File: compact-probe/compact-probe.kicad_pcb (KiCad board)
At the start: 4 copper layers, 47.5 x 47.5 mm, 30 parts, among them J1 Conn_02x05_Counter_Clockwise, J2 SM04B-SRSS-TB(LF)(SN), J3 SM04B-SRSS-TB(LF)(SN), U1 TruStability_SPI, U2 TruStability_SPI, U3 TruStability_SPI, U4 ESP32-C3-WROOM-02-H4, U5 BMP388, U6 LT1963AxST-3.3, X1 baro_cap

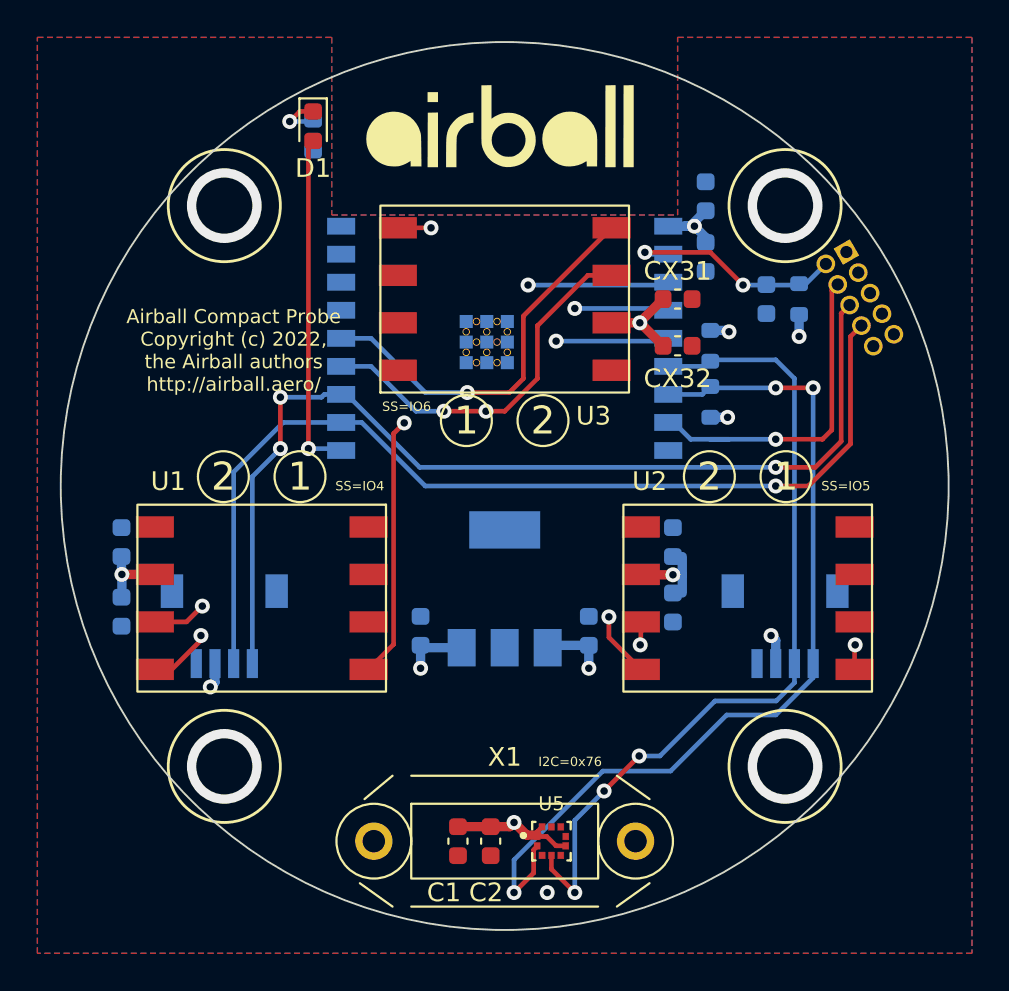
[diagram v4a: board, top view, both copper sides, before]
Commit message: Finished first cut of routing.
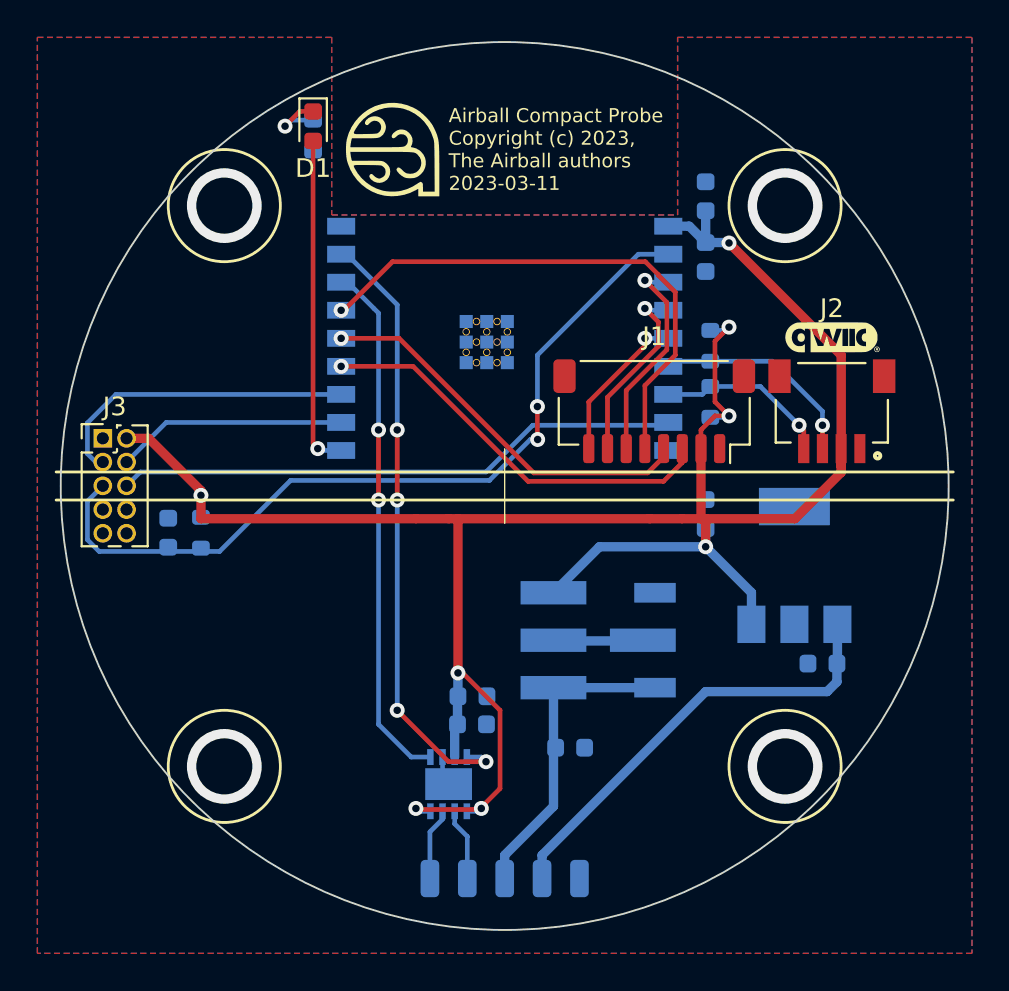
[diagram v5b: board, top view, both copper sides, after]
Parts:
- removed C2, CX12, CX22: 0.1uF, Capacitor_SMD:C_0603_1608Metric
- removed CX11, CX21, CX31, CX32: 4.7uF, Capacitor_SMD:C_0603_1608Metric
- removed the G*** at (-0.15, -18.5)
- removed U1, U2, U3: TruStability_SPI, compact-probe:TruStability SMT
- removed U5: BMP388, compact-probe:BMP388
- removed X1: baro_cap, compact-probe:baro_cap
- added C10: 22uF, Capacitor_SMD:C_0603_1608Metric, B.Cu at (-1.73, 11.2)
- added C9: 100nF, Capacitor_SMD:C_0603_1608Metric, B.Cu at (-1.75, 12.8)
- added G***: LOGO, airball-hardware:airball-logo-5mm, F.Cu at (-6.00, -18.0)
- added IC1: ATA6561-GBQW-N, airball-hardware:SON65P300X300X90-9N-D, B.Cu at (-3.00, 15.9)
- added J4: Conn_01x01_Female, Connector_Wire:SolderWirePad_1x01_SMD_1x2mm, B.Cu at (4.00, 21.0)
- added J5: Conn_01x01_Female, Connector_Wire:SolderWirePad_1x01_SMD_1x2mm, B.Cu at (2.00, 21.0)
- added J6: Conn_01x01_Female, Connector_Wire:SolderWirePad_1x01_SMD_1x2mm, B.Cu at (0.00, 21.0)
- added J7: Conn_01x01_Female, Connector_Wire:SolderWirePad_1x01_SMD_1x2mm, B.Cu at (-2.00, 21.0)
- added J8: Conn_01x01_Female, Connector_Wire:SolderWirePad_1x01_SMD_1x2mm, B.Cu at (-4.00, 21.0)
- added PS1: K7803MT-500R4, airball-hardware:CONV_K7803MT-500R4, B.Cu at (5.00, 8.25)
- C1: value 4.7uF -> 10uF; moved to B.Cu
- G***: moved to F.Cu
- J1: value Conn_02x05_Counter_Clockwise -> Conn_01x08_Male; footprint compact-probe:1.27mm_02x05_header -> airball-hardware:JST_SH_SM08B-SRSS-TB_1x08-1MP_P1.00mm_Horizontal; moved to F.Cu
- J2: value SM04B-SRSS-TB(LF)(SN) -> Conn_01x04_Male; footprint compact-probe:JST_SM04B-SRSS-TB(LF)(SN) -> airball-hardware:JST_SM04B-SRSS-TB(LF)(SN); moved to F.Cu
- J3: value SM04B-SRSS-TB(LF)(SN) -> Conn_02x05_Odd_Even; footprint compact-probe:JST_SM04B-SRSS-TB(LF)(SN) -> Connector_PinHeader_1.27mm:PinHeader_2x05_P1.27mm_Vertical; moved to F.Cu
- moved J3 38.4 mm to (-21.5, -2.55)
- moved J2 34.5 mm to (17.5, -2.00), turned to 180 degrees
- moved C4 34.4 mm to (-18.0, 2.50), turned to 90 degrees
- moved R1 34.4 mm to (-16.2, 2.50), turned to -90 degrees
- moved C5 16.5 mm to (10.8, 1.50)
- moved U6 15.6 mm to (15.5, 4.25)
- moved C3 12.6 mm to (17.0, 9.50), turned to 180 degrees
- moved J1 12.5 mm to (8.00, -4.00), turned to 180 degrees
- moved G*** 11.5 mm to (17.5, -8.00), turned to 0 degrees
- moved C1 7.81 mm to (3.50, 14.0), turned to 0 degrees
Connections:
- C1 pad 1: +3V3 -> 12V28
- C3 pad 1: +5V -> VBAT
- J1 pad 2: unconnected-(J1-Pad2) -> +3V3
- J1 pad 3: unconnected-(J1-Pad3) -> MISO
- J1 pad 4: unconnected-(J1-Pad4) -> SCLK
- J1 pad 5: +5V -> SS1
- J1 pad 6: unconnected-(J1-Pad6) -> SS2
- J1 pad 7: RXD -> SS3
- J1 pad 8: TXD -> SS4
- J2 pad 2: +5V -> +3V3
- J2 pad 3: RXD -> SDA
- J2 pad 4: TXD -> SCL
- J2 pad S1: GND -> (no net)
- J2 pad S2: GND -> (no net)
- J3 pad 3: SDA -> TXD
- J3 pad 4: SCL -> RXD
- U4 pad 15: unconnected-(U4-Pad15) -> SS1
- U4 pad 16: unconnected-(U4-Pad16) -> CAN_TX
- U4 pad 17: unconnected-(U4-Pad17) -> CAN_RX
- U4 pad 3: SS1 -> SS2
- U4 pad 4: SS2 -> SS3
- U4 pad 5: SS3 -> SS4
- U6 pad 1: +5V -> VBAT
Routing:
- net +3V3: track 32.5 -> 121.6 mm, vias 10 -> 8
- net SCLK: track 64.1 -> 21.0 mm, vias 3 -> 1
- net RXD: track 53.7 -> 12.4 mm, vias 1 -> 0
- net SCL: track 48.3 -> 9.39 mm, vias 3 -> 1
- net TXD: track 54.9 -> 16.9 mm, vias 3 -> 0
- net MISO: track 58.5 -> 22.0 mm, vias 4 -> 1
- net SDA: track 44.7 -> 11.5 mm, vias 3 -> 1
- net CAN_RX: track 0.00 -> 32.8 mm, vias 0 -> 4
- net MCU_EN: track 12.2 -> 43.8 mm
- net CAN_TX: track 0.00 -> 28.3 mm, vias 0 -> 2
- net VBAT: track 0.00 -> 24.0 mm
- net SS2: track 30.6 -> 11.7 mm, vias 2 -> 1
- net 12V28: track 0.00 -> 16.7 mm
- net MCU_IO9: track 18.2 -> 30.4 mm, vias 1 -> 0
- net SS3: track 19.5 -> 10.2 mm, vias 2 -> 1
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- removed copper zone on In1.Cu, net +3V3
- removed copper zone on In2.Cu, net +5V
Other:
- copper layers 4 -> 2
- board text added: "12V28"
- board text added: "Airball Compact Probe Copyright (c) 2023, The Airball authors 2023-03-11"
- board text added: "CANH"
- board text added: "CANL"
- board text added: "GND"
- board text added: "VBAT"
- board text removed: "Airball Compact Probe Copyright (c) 2022, the Airball authors http://airball.aero/"
- board text removed: "I2C=0x76"
- board text removed: "SS=IO4"
- board text removed: "SS=IO5"
- board text removed: "SS=IO6"

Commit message: Minor changes.
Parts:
- moved C4 2.02 mm to (-16.2, 1.50), turned to -90 degrees
- moved R1 2.02 mm to (-14.5, 1.50), turned to 90 degrees
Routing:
- net +3V3: track 121.6 -> 126.2 mm
- net MCU_EN: track 43.8 -> 48.2 mm
- net GND: vias 4 -> 5
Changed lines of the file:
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@@
   )
   (footprint "Resistor_SMD:R_0603_1608Metric" (layer "B.Cu")
-    (at -16.25 2.5 -90)
+    (at -14.5 1.5 90)
     (descr "Resistor SMD 0603 (1608 Metric), square (rectangular) end terminal, IPC_7351 nominal, (Body size source: IPC-SM-782 page 72, https://www.pcb-3d.com/wordpress/wp-content/uploads/ipc-sm-782a_amendment_1_and_2.pdf), generated with kicad-footprint-generator")
     (tags "resistor")
@@
     (fp_line (start 0.8 0.4125) (end 0.8 -0.4125) (layer "B.Fab") (width 0.1))
     (fp_line (start -0.8 0.4125) (end 0.8 0.4125) (layer "B.Fab") (width 0.1))
-    (pad "1" smd roundrect (at -0.825 0 270) (size 0.8 0.95) (layers "B.Cu" "B.Paste" "B.Mask") (roundrect_rratio 0.25)
+    (pad "1" smd roundrect (at -0.825 0 90) (size 0.8 0.95) (layers "B.Cu" "B.Paste" "B.Mask") (roundrect_rratio 0.25)
       (net 2 "+3V3") (pintype "passive"))
-    (pad "2" smd roundrect (at 0.825 0 270) (size 0.8 0.95) (layers "B.Cu" "B.Paste" "B.Mask") (roundrect_rratio 0.25)
+    (pad "2" smd roundrect (at 0.825 0 90) (size 0.8 0.95) (layers "B.Cu" "B.Paste" "B.Mask") (roundrect_rratio 0.25)
       (net 3 "MCU_EN") (pintype "passive"))
     (model "${KICAD6_3DMODEL_DIR}/Resistor_SMD.3dshapes/R_0603_1608Metric.wrl"
@@
   )
   (footprint "Capacitor_SMD:C_0603_1608Metric" (layer "B.Cu")
-    (at -18 2.5 90)
+    (at -16.25 1.5 -90)
     (descr "Capacitor SMD 0603 (1608 Metric), square (rectangular) end terminal, IPC_7351 nominal, (Body size source: IPC-SM-782 page 76, https://www.pcb-3d.com/wordpress/wp-content/uploads/ipc-sm-782a_amendment_1_and_2.pdf), generated with kicad-footprint-generator")
     (tags "capacitor")
@@
     (fp_line (start 0.8 0.4) (end 0.8 -0.4) (layer "B.Fab") (width 0.1))
     (fp_line (start -0.8 0.4) (end 0.8 0.4) (layer "B.Fab") (width 0.1))
-    (pad "1" smd roundrect (at -0.775 0 90) (size 0.9 0.95) (layers "B.Cu" "B.Paste" "B.Mask") (roundrect_rratio 0.25)
+    (pad "1" smd roundrect (at -0.775 0 270) (size 0.9 0.95) (layers "B.Cu" "B.Paste" "B.Mask") (roundrect_rratio 0.25)
       (net 3 "MCU_EN") (pintype "passive"))
-    (pad "2" smd roundrect (at 0.775 0 90) (size 0.9 0.95) (layers "B.Cu" "B.Paste" "B.Mask") (roundrect_rratio 0.25)
+    (pad "2" smd roundrect (at 0.775 0 270) (size 0.9 0.95) (layers "B.Cu" "B.Paste" "B.Mask") (roundrect_rratio 0.25)
       (net 1 "GND") (pintype "passive"))
     (model "${KICAD6_3DMODEL_DIR}/Capacitor_SMD.3dshapes/C_0603_1608Metric.wrl"
@@
   (via locked (at 15 -15) (size 4) (drill 3) (layers "F.Cu" "B.Cu") (free) (net 1))
   (via locked (at -15 15) (size 4) (drill 3) (layers "F.Cu" "B.Cu") (free) (net 1))
+  (via (at -19.75 -3.75) (size 0.8) (drill 0.4) (layers "F.Cu" "B.Cu") (free) (net 1))
   (via locked (at 15 15) (size 4) (drill 3) (layers "F.Cu" "B.Cu") (free) (net 1))
   (via locked (at -15 -15) (size 4) (drill 3) (layers "F.Cu" "B.Cu") (free) (net 1))
@@
   (segment (start 10.75 1.75) (end 10.5 1.75) (width 0.5) (layer "F.Cu") (net 2))
   (segment (start -2.5 10) (end -2.25 10) (width 0.25) (layer "F.Cu") (net 2))
+  (segment (start -16.75 -0.25) (end -19.05 -2.55) (width 0.5) (layer "F.Cu") (net 2))
+  (segment (start -16.25 0.25) (end -16.75 -0.25) (width 0.5) (layer "F.Cu") (net 2))
   (segment (start 9.5 1.75) (end 7.75 1.75) (width 0.5) (layer "F.Cu") (net 2))
   (segment (start 10.5 -2) (end 10.475 -1.975) (width 0.5) (layer "F.Cu") (net 2))
@@
   (segment (start 18 -2) (end 18 -0.725) (width 0.5) (layer "F.Cu") (net 2))
   (segment (start 18 -1) (end 18 -2) (width 0.5) (layer "F.Cu") (net 2))
-  (segment (start -16.25 0.5) (end -16.25 0.25) (width 0.5) (layer "F.Cu") (net 2))
   (segment (start 10.75 3.25) (end 10.75 1.75) (width 0.5) (layer "F.Cu") (net 2))
+  (segment (start -11 1.75) (end -14.75 1.75) (width 0.5) (layer "F.Cu") (net 2))
   (segment (start -4.75 1.75) (end -3 1.75) (width 0.5) (layer "F.Cu") (net 2))
   (segment (start -3 1.75) (end -2.5 1.75) (width 0.5) (layer "F.Cu") (net 2))
+  (segment (start -11 1.75) (end -4.75 1.75) (width 0.5) (layer "F.Cu") (net 2))
   (segment (start 18 -7) (end 12 -13) (width 0.5) (layer "F.Cu") (net 2))
   (segment (start 12 -3.75) (end 11.25 -3.75) (width 0.25) (layer "F.Cu") (net 2))
+  (segment (start -14.75 1.75) (end -16.75 -0.25) (width 0.5) (layer "F.Cu") (net 2))
   (segment (start 12 -3.75) (end 11.25 -4.5) (width 0.25) (layer "F.Cu") (net 2))
   (segment (start -0.25 16.188055) (end -1.370321 17.308376) (width 0.25) (layer "F.Cu") (net 2))
   (segment (start -19.05 -2.55) (end -20.23 -2.55) (width 0.5) (layer "F.Cu") (net 2))
+  (segment (start -14.5 3.25) (end -14.5 1.75) (width 0.25) (layer "F.Cu") (net 2))
   (segment (start 11.25 -3.75) (end 10.5 -3) (width 0.25) (layer "F.Cu") (net 2))
   (segment (start 10.5 1.75) (end 9.5 1.75) (width 0.5) (layer "F.Cu") (net 2))
   (segment (start -0.25 12) (end -0.25 16.188055) (width 0.25) (layer "F.Cu") (net 2))
   (segment (start 10.5 -2) (end 10.5 1.75) (width 0.5) (layer "F.Cu") (net 2))
-  (segment (start -16.25 0.25) (end -19.05 -2.55) (width 0.5) (layer "F.Cu") (net 2))
   (segment (start 15.525 1.75) (end 10.75 1.75) (width 0.5) (layer "F.Cu") (net 2))
+  (segment (start -14.5 1.75) (end -11 1.75) (width 0.5) (layer "F.Cu") (net 2))
   (segment (start -2.25 10) (end -0.25 12) (width 0.25) (layer "F.Cu") (net 2))
   (segment (start 18 -0.725) (end 15.525 1.75) (width 0.5) (layer "F.Cu") (net 2))
-  (segment (start -16.25 1.75) (end -4.75 1.75) (width 0.5) (layer "F.Cu") (net 2))
   (segment (start -2.5 10) (end -2.5 1.75) (width 0.5) (layer "F.Cu") (net 2))
   (segment (start 11.25 -4.5) (end 11.25 -7.75) (width 0.25) (layer "F.Cu") (net 2))
@@
   (segment (start -1.370321 17.308376) (end -4.567735 17.308376) (width 0.25) (layer "F.Cu") (net 2))
   (segment (start -2.5 1.75) (end 7.75 1.75) (width 0.5) (layer "F.Cu") (net 2))
-  (segment (start -16.25 0.5) (end -16.25 1.75) (width 0.5) (layer "F.Cu") (net 2))
   (via (at 10.75 3.25) (size 0.8) (drill 0.4) (layers "F.Cu" "B.Cu") (net 2))
   (via (at 12 -8.5) (size 0.8) (drill 0.4) (layers "F.Cu" "B.Cu") (net 2))
-  (via (at -16.25 0.5) (size 0.8) (drill 0.4) (layers "F.Cu" "B.Cu") (net 2))
   (via (at 12 -13) (size 0.8) (drill 0.4) (layers "F.Cu" "B.Cu") (net 2))
   (via (at 12 -3.75) (size 0.8) (drill 0.4) (layers "F.Cu" "B.Cu") (net 2))
   (via (at -1.25 17.25) (size 0.8) (drill 0.4) (layers "F.Cu" "B.Cu") (net 2))
   (via (at -2.5 10) (size 0.8) (drill 0.4) (layers "F.Cu" "B.Cu") (net 2))
+  (via (at -14.5 3.25) (size 0.8) (drill 0.4) (layers "F.Cu" "B.Cu") (net 2))
   (via (at -4.75 17.25) (size 0.8) (drill 0.4) (layers "F.Cu" "B.Cu") (net 2))
   (segment (start 10.75 3.25) (end 5.07 3.25) (width 0.5) (layer "B.Cu") (net 2))
@@
   (segment (start -2.675 14.5) (end -2.675 12.9) (width 0.5) (layer "B.Cu") (net 2))
   (segment (start 9.875 -13.9) (end 10.75 -13.025) (width 0.5) (layer "B.Cu") (net 2))
-  (segment (start -16.25 1.675) (end -16.25 0.5) (width 0.25) (layer "B.Cu") (net 2))
+  (segment (start -14.5 2.325) (end -14.5 3.25) (width 0.25) (layer "B.Cu") (net 2))
   (segment (start 8.75 -13.9) (end 9.875 -13.9) (width 0.5) (layer "B.Cu") (net 2))
   (segment (start 5.07 3.25) (end 2.61 5.71) (width 0.5) (layer "B.Cu") (net 2))
@@
   (via (at 1.762299 -2.487701) (size 0.8) (drill 0.4) (layers "F.Cu" "B.Cu") (net 3))
   (via (at 1.75 -4.25) (size 0.8) (drill 0.4) (layers "F.Cu" "B.Cu") (net 3))
+  (segment (start -16.2 0.675) (end -16.25 0.725) (width 0.25) (layer "B.Cu") (net 3))
   (segment (start 7.15 -12.4) (end 8.75 -12.4) (width 0.25) (layer "B.Cu") (net 3))
-  (segment (start -0.813604 -0.3) (end -11.45 -0.3) (width 0.25) (layer "B.Cu") (net 3))
+  (segment (start -16.25 0.725) (end -16.25 -0.25) (width 0.25) (layer "B.Cu") (net 3))
+  (segment (start 1.762299 -2.487701) (end 1.374097 -2.487701) (width 0.25) (layer "B.Cu") (net 3))
+  (segment (start 1.75 -4.25) (end 1.75 -7) (width 0.25) (layer "B.Cu") (net 3))
+  (segment (start -21.696727 3.5) (end -22.325 2.871727) (width 0.25) (layer "B.Cu") (net 3))
+  (segment (start -14.5 0.675) (end -16.2 0.675) (width 0.25) (layer "B.Cu") (net 3))
   (segment (start -22.325 0.815) (end -21.5 -0.01) (width 0.25) (layer "B.Cu") (net 3))
+  (segment (start -19.405 0.155) (end -19.405 2.871727) (width 0.25) (layer "B.Cu") (net 3))
+  (segment (start -22.325 2.871727) (end -22.325 0.815) (width 0.25) (layer "B.Cu") (net 3))
   (segment (start 1.374097 -2.487701) (end -0.813604 -0.3) (width 0.25) (layer "B.Cu") (net 3))
-  (segment (start 1.75 -4.25) (end 1.75 -7) (width 0.25) (layer "B.Cu") (net 3))
-  (segment (start -15.25 3.5) (end -21.696727 3.5) (width 0.25) (layer "B.Cu") (net 3))
-  (segment (start 1.762299 -2.487701) (end 1.374097 -2.487701) (width 0.25) (layer "B.Cu") (net 3))
-  (segment (start -22.325 2.871727) (end -22.325 0.815) (width 0.25) (layer "B.Cu") (net 3))
-  (segment (start -21.696727 3.5) (end -22.325 2.871727) (width 0.25) (layer "B.Cu") (net 3))
+  (segment (start -0.813604 -0.3) (end -16.2 -0.3) (width 0.25) (layer "B.Cu") (net 3))
+  (segment (start -16.2 -0.3) (end -18.95 -0.3) (width 0.25) (layer "B.Cu") (net 3))
   (segment (start 1.75 -7) (end 7.15 -12.4) (width 0.25) (layer "B.Cu") (net 3))
-  (segment (start -11.45 -0.3) (end -15.25 3.5) (width 0.25) (layer "B.Cu") (net 3))
+  (segment (start -20.033273 3.5) (end -21.696727 3.5) (width 0.25) (layer "B.Cu") (net 3))
+  (segment (start -16.25 -0.25) (end -16.2 -0.3) (width 0.25) (layer "B.Cu") (net 3))
+  (segment (start -18.95 -0.3) (end -19.405 0.155) (width 0.25) (layer "B.Cu") (net 3))
+  (segment (start -19.405 2.871727) (end -20.033273 3.5) (width 0.25) (layer "B.Cu") (net 3))
   (segment (start -10.9625 -20.0375) (end -11.75 -19.25) (width 0.25) (layer "F.Cu") (net 4))
   (segment (start -10.25 -20.0375) (end -10.9625 -20.0375) (width 0.25) (layer "F.Cu") (net 4))
